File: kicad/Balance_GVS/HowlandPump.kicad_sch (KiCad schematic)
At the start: 0 parts

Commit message: Started adding howland connections
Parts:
- added R2: 100k, symbol Device:R
- added R3, R7: 50k, symbol Device:R
- added R35, R38: 10k, symbol Device:R
- added R36: 100, symbol Device:R
- added R37: 10, symbol Device:R
- added U11, U12: LT1013DIP, LT1013DIP:DIP794W45P254L959H508Q8, symbol LT1013DIP:LT1013DIP
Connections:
- new net: R36.1, R37.2
- new net: R3.2, R35.1, U11.6 (2IN-)
- new net: R35.2, R36.2, U11.7 (2OUT)
- new net 1.65V: R2.2, R3.1
- new net 1IN-: R7.1, U11.1 (1OUT), U11.2 (1IN-)
- new net 2IN+: R38.1, R7.2, U11.5 (2IN+)
- new net DAC_OUT: R2.1, U11.3 (1IN_+)
- new net GND: U11.4 (VCC-), U12.4 (VCC-)
- new net Howland_Supply_Rail: U11.8 (VCC+), U12.8 (VCC+)
- new net OUT1: R38.2, U12.1 (1OUT), U12.2 (1IN-)
- new net Safety+: R37.1, U12.3 (1IN_+)

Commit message: Finish Howland
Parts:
- added R39, R40, R41, R42: 10k, symbol Device:R
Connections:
- net GND: now also R42.1
- net Safety-: now also U12.7 (2OUT), R39.2
- net 12V: now reaches U12.5 (2IN+)
- net 12V: now also R41.1, R42.2
- net at U12.6 (2IN-): now also R39.1, R40.1
- net Howland_Supply_Rail renamed 24V
- net 24V: now also R41.2
- net OUT1 renamed 3IN-
- net 3IN-: now also R40.2
- net Safety+ renamed Electrode+
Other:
- moved on the sheet: R35

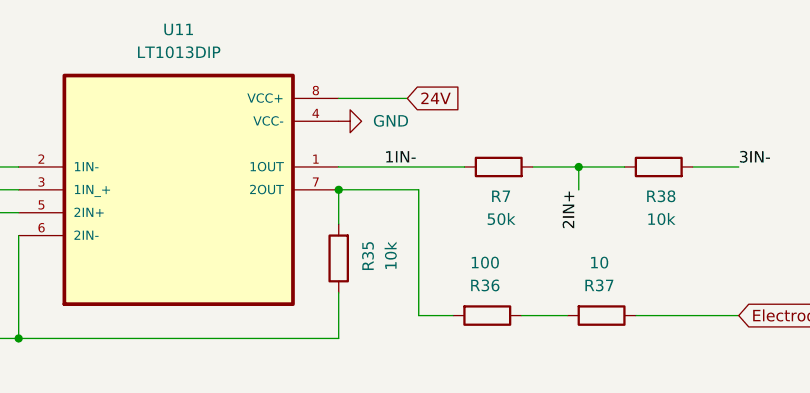
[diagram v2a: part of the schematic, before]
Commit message: Add Footprints to Schematic
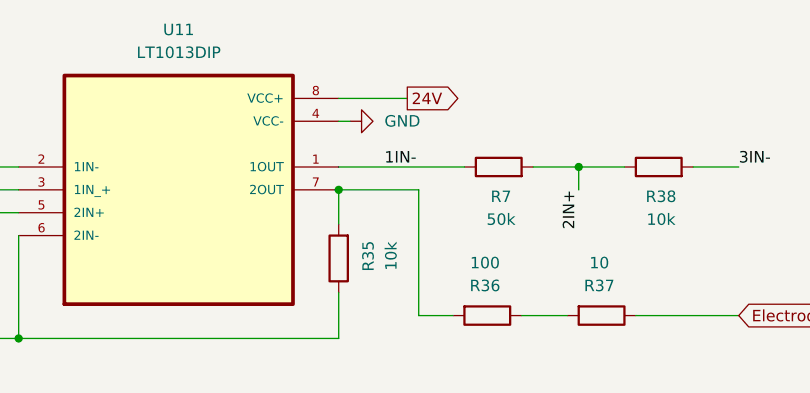
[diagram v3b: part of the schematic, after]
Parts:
- R2, R3, R35, R36, R37, R38, R39, R40, R41, R42, R7: footprint (none) -> Resistor_SMD:R_0805_2012Metric_Pad1.20x1.40mm_HandSolder
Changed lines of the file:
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@@
+	(wire
+		(pts
+			(xy 130.81 76.2) (xy 129.54 76.2)
+		)
+		(stroke
+			(width 0)
+			(type default)
+		)
+	)
 	(wire
 		(pts
@@
 	)
 	(global_label "24V"
-		(shape input)
+		(shape output)
 		(at 137.16 73.66 0)
 		(fields_autoplaced yes)
@@
 			)
 		)
-		(property "Footprint" ""
+		(property "Footprint" "Resistor_SMD:R_0805_2012Metric_Pad1.20x1.40mm_HandSolder"
 			(at 143.51 150.368 90)
 			(hide yes)
@@
 			)
 		)
-		(property "Footprint" ""
+		(property "Footprint" "Resistor_SMD:R_0805_2012Metric_Pad1.20x1.40mm_HandSolder"
 			(at 158.75 96.012 90)
 			(hide yes)
@@
 			)
 		)
-		(property "Footprint" ""
+		(property "Footprint" "Resistor_SMD:R_0805_2012Metric_Pad1.20x1.40mm_HandSolder"
 			(at 57.658 128.27 90)
 			(hide yes)
@@
 			)
 		)
-		(property "Footprint" ""
+		(property "Footprint" "Resistor_SMD:R_0805_2012Metric_Pad1.20x1.40mm_HandSolder"
 			(at 131.318 91.44 90)
 			(hide yes)
@@
 			)
 		)
-		(property "Footprint" ""
+		(property "Footprint" "Resistor_SMD:R_0805_2012Metric_Pad1.20x1.40mm_HandSolder"
 			(at 147.32 83.058 90)
 			(hide yes)
@@
 	(symbol
 		(lib_id "power:GND")
-		(at 129.54 76.2 90)
+		(at 130.81 76.2 90)
 		(unit 1)
 		(body_style 1)
@@
 		(fields_autoplaced yes)
 		(property "Reference" "#PWR01"
-			(at 135.89 76.2 0)
+			(at 137.16 76.2 0)
 			(hide yes)
 			(show_name no)
@@
 		)
 		(property "Value" "GND"
-			(at 133.35 76.1999 90)
+			(at 134.62 76.1999 90)
 			(show_name no)
 			(do_not_autoplace no)
@@
 		)
 		(property "Footprint" ""
-			(at 129.54 76.2 0)
+			(at 130.81 76.2 0)
 			(hide yes)
 			(show_name no)
@@
 		)
 		(property "Datasheet" ""
-			(at 129.54 76.2 0)
+			(at 130.81 76.2 0)
 			(hide yes)
 			(show_name no)
@@
 		)
 		(property "Description" "Power symbol creates a global label with name \"GND\" , ground"
-			(at 129.54 76.2 0)
+			(at 130.81 76.2 0)
 			(hide yes)
 			(show_name no)
@@
 			)
 		)
-		(property "Footprint" ""
+		(property "Footprint" "Resistor_SMD:R_0805_2012Metric_Pad1.20x1.40mm_HandSolder"
 			(at 133.858 140.97 90)
 			(hide yes)
@@
 			)
 		)
-		(property "Footprint" ""
+		(property "Footprint" "Resistor_SMD:R_0805_2012Metric_Pad1.20x1.40mm_HandSolder"
 			(at 69.342 90.17 90)
 			(hide yes)
@@
 			)
 		)
-		(property "Footprint" ""
+		(property "Footprint" "Resistor_SMD:R_0805_2012Metric_Pad1.20x1.40mm_HandSolder"
 			(at 57.658 139.7 90)
 			(hide yes)
@@
 			)
 		)
-		(property "Footprint" ""
+		(property "Footprint" "Resistor_SMD:R_0805_2012Metric_Pad1.20x1.40mm_HandSolder"
 			(at 165.1 83.058 90)
 			(hide yes)
@@
 			)
 		)
-		(property "Footprint" ""
+		(property "Footprint" "Resistor_SMD:R_0805_2012Metric_Pad1.20x1.40mm_HandSolder"
 			(at 146.05 96.012 90)
 			(hide yes)
@@
 			)
 		)
-		(property "Footprint" ""
+		(property "Footprint" "Resistor_SMD:R_0805_2012Metric_Pad1.20x1.40mm_HandSolder"
 			(at 83.82 102.108 90)
 			(hide yes)

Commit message: Add shit ton to schematic
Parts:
- added C26: 10nF, Capacitor_SMD:C_0805_2012Metric_Pad1.18x1.45mm_HandSolder, symbol Device:C
- added R52: 10k, Resistor_SMD:R_0805_2012Metric_Pad1.20x1.40mm_HandSolder, symbol Device:R
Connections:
- net DAC_OUT: now also R52.2; no longer U11.3 (1IN_+)
- net GND: now also C26.2
- net Safety- renamed Current_Sense-
- new net: C26.1, R52.1, U11.3 (1IN_+)

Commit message: Fixed schematic warnings
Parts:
- added J11: Conn_01x02_Pin, Connector_PinSocket_2.54mm:PinSocket_1x02_P2.54mm_Vertical, symbol Connector:Conn_01x02_Pin
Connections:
- net GND: now also J11.1 (Pin_1)
- net 24V renamed +24V
- net +24V: now also J11.2 (Pin_2)

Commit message: I kinda popped off ngl. Main pcb almost done
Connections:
- net 1.65V renamed VREF
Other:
- moved on the sheet: R41
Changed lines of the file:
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@@
-		)
-	)
-	(global_label "1.65V"
-		(shape input)
-		(at 71.12 104.14 270)
-		(fields_autoplaced yes)
-		(effects
-			(font
-				(size 1.27 1.27)
-			)
-			(justify right)
-		)
-		(property "Intersheetrefs" "${INTERSHEET_REFS}"
-			(at 71.12 112.4471 90)
-			(hide yes)
-			(show_name no)
-			(do_not_autoplace no)
-			(effects
-				(font
-					(size 1.27 1.27)
-				)
-				(justify right)
-			)
 		)
 	)
@@
 		)
 	)
+	(global_label "VREF"
+		(shape input)
+		(at 71.12 104.14 270)
+		(fields_autoplaced yes)
+		(effects
+			(font
+				(size 1.27 1.27)
+			)
+			(justify right)
+		)
+		(property "Intersheetrefs" "${INTERSHEET_REFS}"
+			(at 71.12 111.7214 90)
+			(hide yes)
+			(show_name no)
+			(do_not_autoplace no)
+			(effects
+				(font
+					(size 1.27 1.27)
+				)
+				(justify right)
+			)
+		)
+	)
 	(symbol
 		(lib_id "Device:R")
@@
 	(symbol
 		(lib_id "Device:R")
-		(at 55.88 128.27 180)
+		(at 55.88 128.27 0)
+		(mirror x)
 		(unit 1)
 		(body_style 1)
@@
 		(dnp no)
 		(property "Reference" "R41"
-			(at 59.182 128.016 90)
+			(at 52.578 128.016 90)
 			(show_name no)
 			(do_not_autoplace no)
@@
 		)
 		(property "Value" "10k"
-			(at 61.722 128.016 90)
+			(at 50.038 128.016 90)
 			(show_name no)
 			(do_not_autoplace no)
@@
 		)
 		(property "Footprint" "Resistor_SMD:R_0805_2012Metric_Pad1.20x1.40mm_HandSolder"
-			(at 57.658 128.27 90)
-			(hide yes)
-			(show_name no)
+			(at 54.102 128.27 90)
+			(hide yes)
+			(show_name no)

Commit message: Final Main PCB!
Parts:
- added C2, C3: 100nF, Capacitor_SMD:C_0805_2012Metric_Pad1.18x1.45mm_HandSolder, symbol Device:C
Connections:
- net +24V: now also C2.1, C3.1
- net GND: now also C2.2, C3.2
